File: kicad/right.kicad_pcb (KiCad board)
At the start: 4 copper layers, 137.5 x 109.3 mm, 114 parts, among them Q1 PMF170XP,115, Q2 FS8205A_C2830320, SW1 TS-1088-AR02016, U1 SN74LVC1G17DBVR, U10 SN74LVC1G74DQER, U2 E73-2G4M08S1C, U4 S2B-PH-K-S(LF)(SN), U5 BL8573CS8TR, U6 DW01A_C42380662, U7 LP5024RSMR, U8 MAX17048, U9 USBLC6-2SC6, X1 FC-13532.768KHZ9PF20PPM

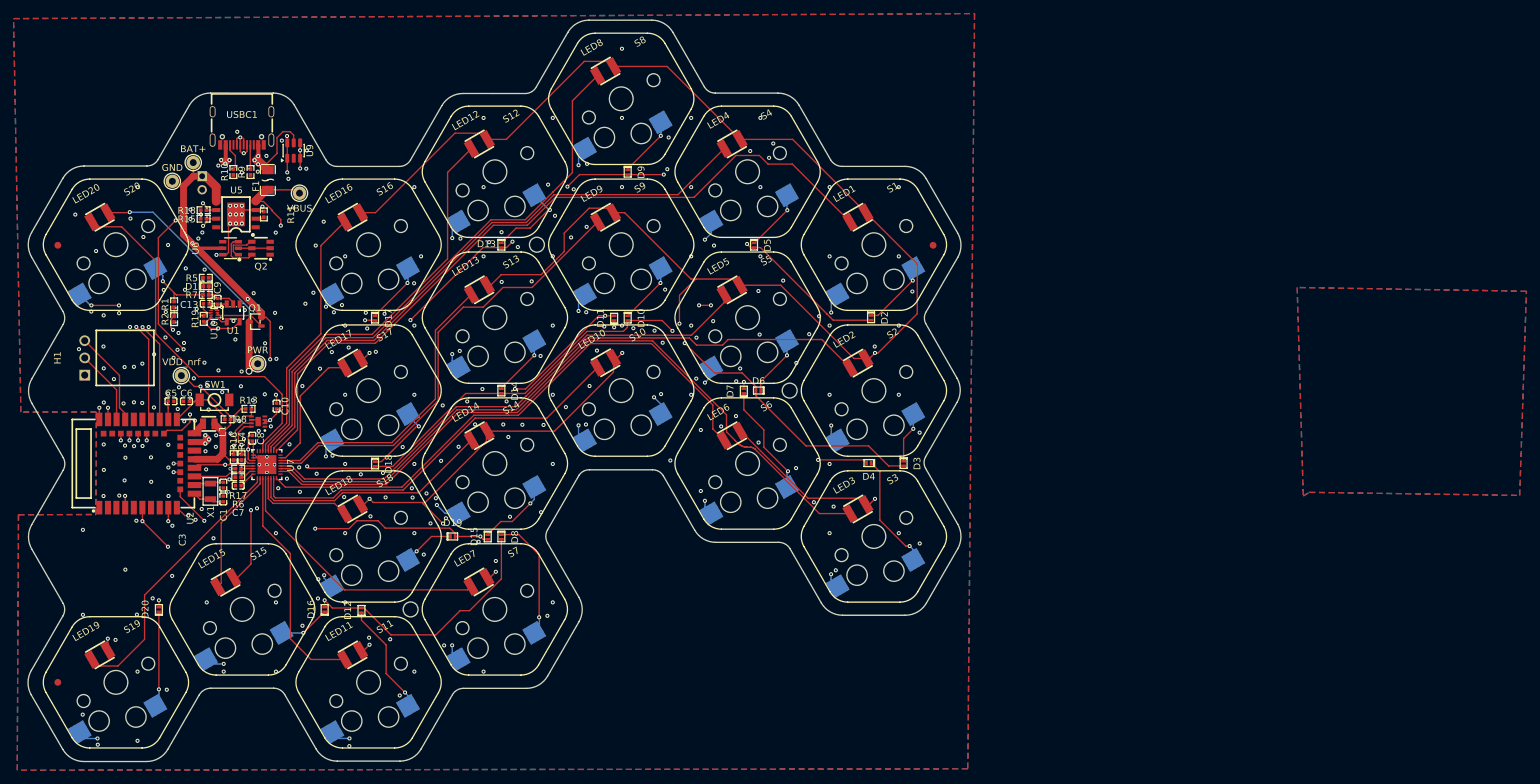
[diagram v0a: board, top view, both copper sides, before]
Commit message: rewired and finalized right side. updated panel. changed dnp of some components on both sides
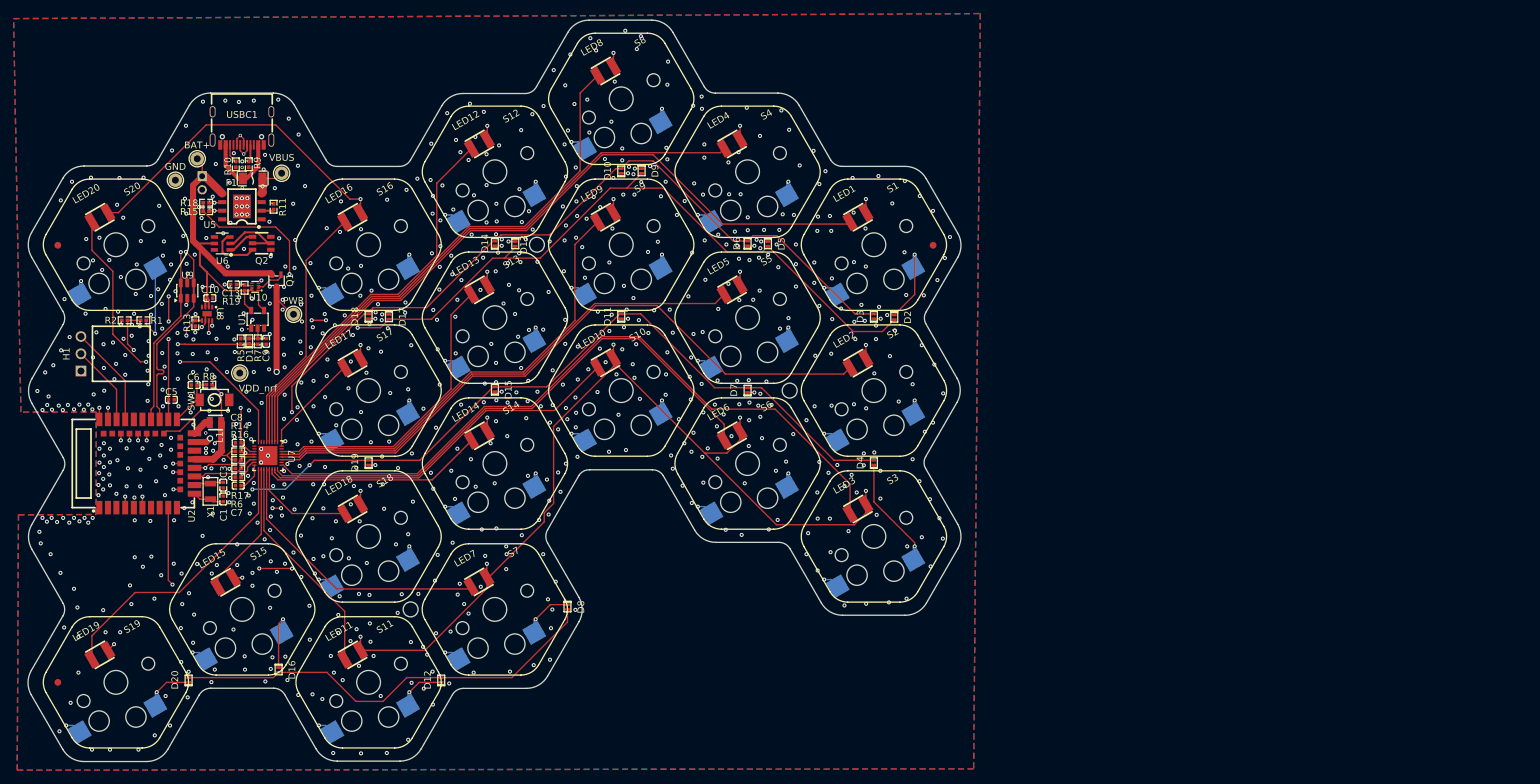
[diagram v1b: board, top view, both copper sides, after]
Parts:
- C1, C3: value 0402CG120F500NT -> 0402CG120J500NT
- moved U9 25.9 mm to (59.4, 58.9)
- moved D3 22.1 mm to (160.6, 62.7), turned to 90 degrees
- moved D15 21.8 mm to (104.8, 73.4), turned to 90 degrees
- moved D14 21.8 mm to (104.8, 51.9), turned to 90 degrees
- moved D18 21.8 mm to (86.2, 62.7), turned to 90 degrees
- moved D6 21.7 mm to (142.0, 51.9), turned to 90 degrees
- moved D10 21.7 mm to (123.4, 41.3), turned to 90 degrees
- moved C10 18.7 mm to (62.8, 60.0), turned to 0 degrees
- moved U8 17.6 mm to (62.4, 62.3), turned to -90 degrees
- moved D19 16.5 mm to (86.2, 84.3), turned to 90 degrees
- moved D12 15.6 mm to (96.9, 116.3)
- moved R13 14.9 mm to (60.6, 63.7), turned to -90 degrees
- moved D8 14.2 mm to (115.5, 105.5)
- moved D20 11.3 mm to (59.6, 116.3)
- moved D16 11.2 mm to (72.9, 114.8), turned to -90 degrees
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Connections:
- U7 pad 10: /LED3 -> unconnected-(U7-OUT9-Pad10)
- U7 pad 15: /LED17 -> unconnected-(U7-OUT14-Pad15)
- U7 pad 16: unconnected-(U7-OUT15-Pad16) -> /LED17
- U7 pad 22: /LED20 -> unconnected-(U7-OUT21-Pad22)
- U7 pad 24: unconnected-(U7-OUT23-Pad24) -> /LED20
- U7 pad 9: unconnected-(U7-OUT8-Pad9) -> /LED3
- U9 pad 5: /VBUS_RAW -> /VBUS
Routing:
- net /PWR: track 537.2 -> 596.5 mm, vias 17 -> 22
- net /ROW3: track 147.9 -> 123.4 mm, vias 9 -> 3
- net /VBUS_RAW: track 32.5 -> 12.6 mm, vias 6 -> 0
- net /COL2: track 235.4 -> 255.1 mm
- net GND: track 21.3 -> 1.93 mm, vias 299 -> 833
- net /SDA: track 22.8 -> 41.7 mm, vias 2 -> 3
- net /D-: track 67.8 -> 50.3 mm, vias 4 -> 2
- net /D+: track 66.6 -> 50.5 mm, vias 4 -> 2
- net /PWR_BTN: track 13.0 -> 26.9 mm, vias 1 -> 2
- net /VDD_nRF: track 61.2 -> 74.8 mm, vias 4 -> 3
- net /ROW2: track 129.9 -> 143.5 mm
- net /SCL: track 19.0 -> 32.0 mm
- net /COL4: track 165.4 -> 176.3 mm
- net /ROW4: track 80.7 -> 90.9 mm, vias 3 -> 2
- net Net-(D8-Pad1): track 17.6 -> 7.68 mm
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
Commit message: experiment
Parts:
- moved R11 0.86 mm to (72.8, 47.1), turned to 180 degrees
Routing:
- net GND: vias 833 -> 834

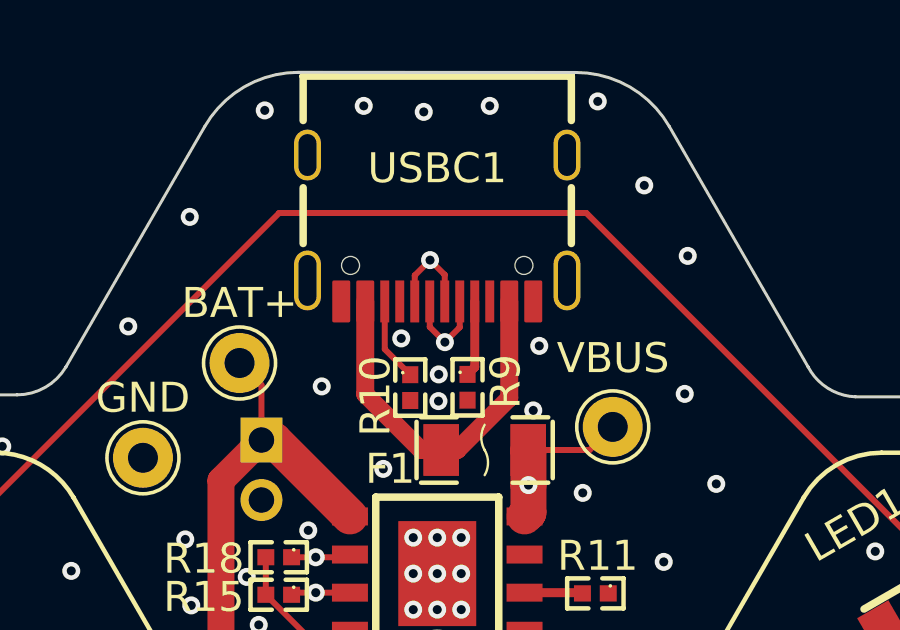
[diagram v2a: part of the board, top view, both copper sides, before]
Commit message: plan for changing charger. reason = heat
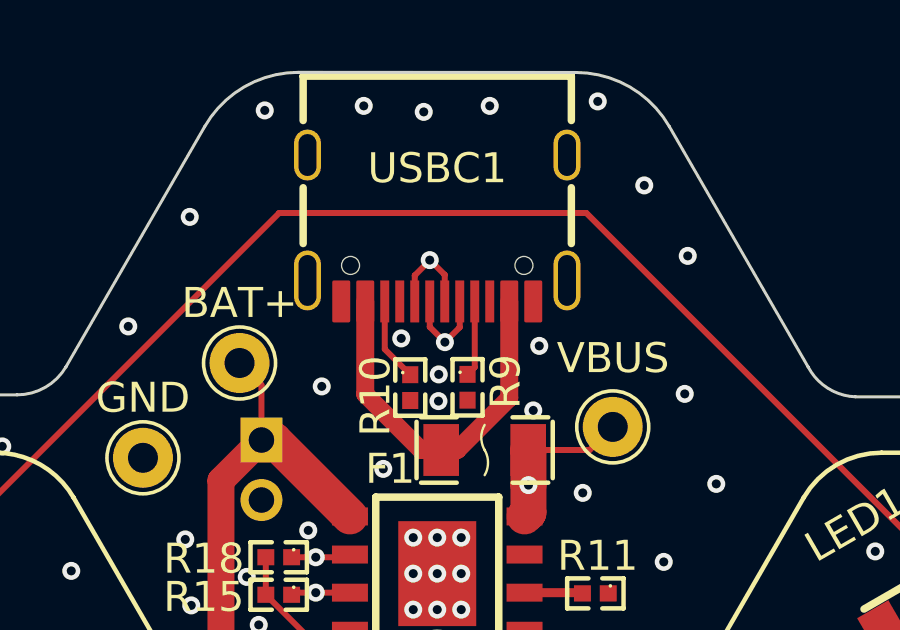
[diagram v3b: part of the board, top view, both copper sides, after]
